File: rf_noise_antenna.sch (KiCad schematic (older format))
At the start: 41 parts, among them J1 Conn_Coaxial, J2 Conn_Coaxial, J3 Conn_01x03, J4 Raspberry_Pi_2_3, K1 MASWSS0115, K2 MASWSS0115, Q1 BC817, Q2 BC817, T1 MABA-009180-500MHz_1P_1S, U1 L7809

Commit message: Added measurmets
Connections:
- net at C11.1, C13.1, L4.2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: now also J3.2 (Pin_2); no longer J3.3 (Pin_3)
- net at C12.1, U1.1 (IN): now also J3.3 (Pin_3); no longer J3.2 (Pin_2)
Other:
- note added: "12V Power supply \nfor Active Antenna."
- note removed: "12V Powersupply for\n Active Antenna"
- moved on the sheet: C1, C10, C11, C12, C13, C14, C15, C2, C3, C4, C5, C6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

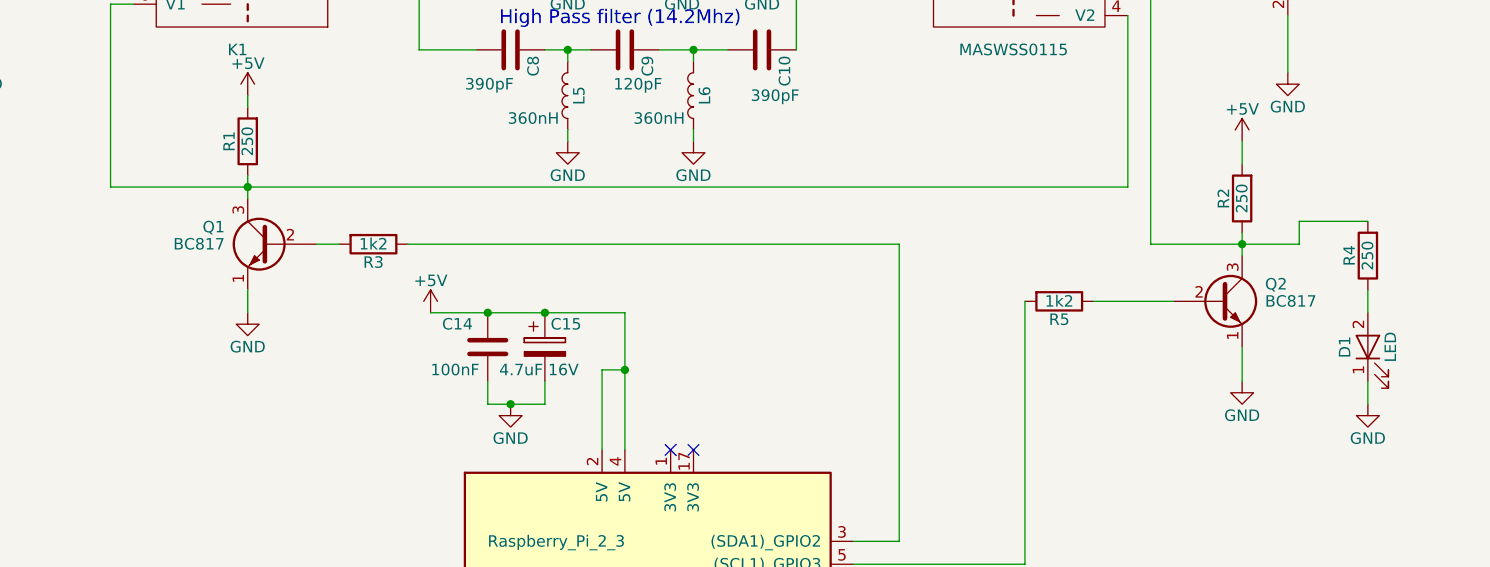
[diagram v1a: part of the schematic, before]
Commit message: Fix Transistor pin config
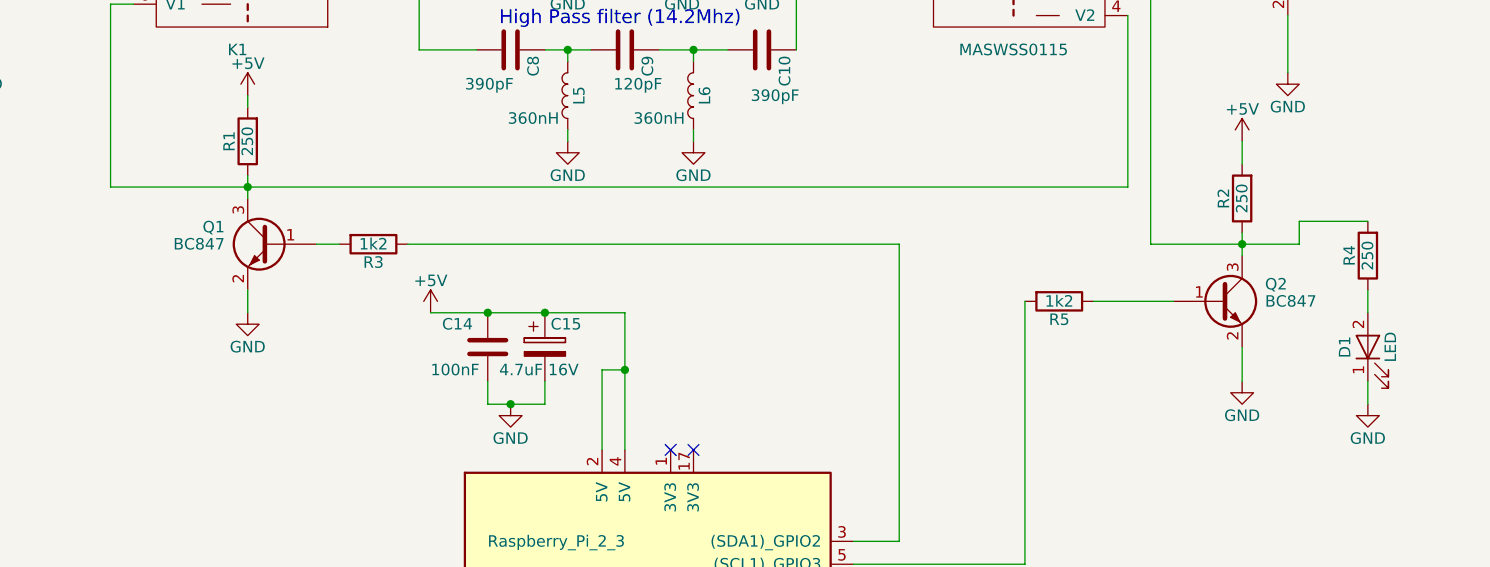
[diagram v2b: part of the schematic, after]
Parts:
- removed Q1, Q2: BC817, TO_SOT_Packages_SMD:SOT-23, symbol 2N2219
- added Q1, Q2: BC847, TO_SOT_Packages_SMD:SOT-23, symbol BC847
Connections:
- net GND: now also Q1.2 (E), Q2.2 (E)
- net at R5.1: now also Q2.1 (B)
- net at K1.4 (V2), K2.6 (V1), R2.1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: now also Q2.3 (C)
- net at K1.6 (V1), K2.4 (V2), R1.1: now also Q1.3 (C)
- net at R3.2: now also Q1.1 (B)
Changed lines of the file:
@@
-$EndComp
-$Comp
-L 2N2219 Q2
-U 1 1 5B76B57A
-P 9900 2650
-F 0 "Q2" H 10100 2725 50  0000 L CNN
-F 1 "BC817" H 10100 2650 50  0000 L CNN
-F 2 "TO_SOT_Packages_SMD:SOT-23" H 10100 2575 50  0001 L CIN
-F 3 "" H 9900 2650 50  0001 L CNN
-	1    9900 2650
-	1    0    0    -1
 $EndComp
 $Comp
@@
 $EndComp
 $Comp
-L 2N2219 Q1
-U 1 1 5B79A333
-P 5750 2400
-F 0 "Q1" H 5950 2475 50  0000 L CNN
-F 1 "BC817" H 5950 2400 50  0000 L CNN
-F 2 "TO_SOT_Packages_SMD:SOT-23" H 5950 2325 50  0001 L CIN
-F 3 "" H 5750 2400 50  0001 L CNN
-	1    5750 2400
-	-1   0    0    -1
-$EndComp
-$Comp
 L R R2
 U 1 1 5B79AFBD
@@
 Wire Wire Line
 	2050 1950 2250 1950
+$Comp
+L BC847 Q1
+U 1 1 5B831B5C
+P 5750 2400
+F 0 "Q1" H 5950 2475 50  0000 L CNN
+F 1 "BC847" H 5950 2400 50  0000 L CNN
+F 2 "TO_SOT_Packages_SMD:SOT-23" H 5950 2325 50  0001 L CIN
+F 3 "" H 5750 2400 50  0001 L CNN
+	1    5750 2400
+	-1   0    0    -1
+$EndComp
+$Comp
+L BC847 Q2
+U 1 1 5B83282F
+P 9900 2650
+F 0 "Q2" H 10100 2725 50  0000 L CNN
+F 1 "BC847" H 10100 2650 50  0000 L CNN
+F 2 "TO_SOT_Packages_SMD:SOT-23" H 10100 2575 50  0001 L CIN
+F 3 "" H 9900 2650 50  0001 L CNN
+	1    9900 2650
+	1    0    0    -1
+$EndComp
 $EndSCHEMATC

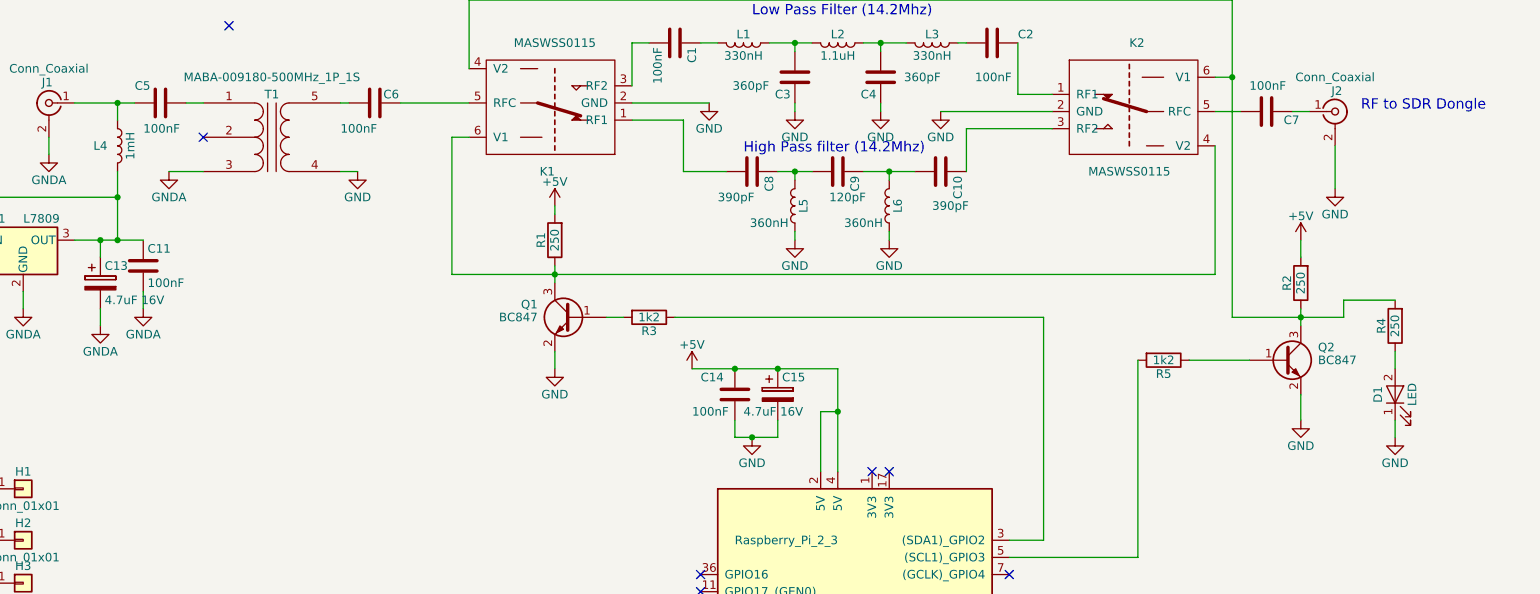
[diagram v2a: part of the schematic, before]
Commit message: Fix LED and Inductor value
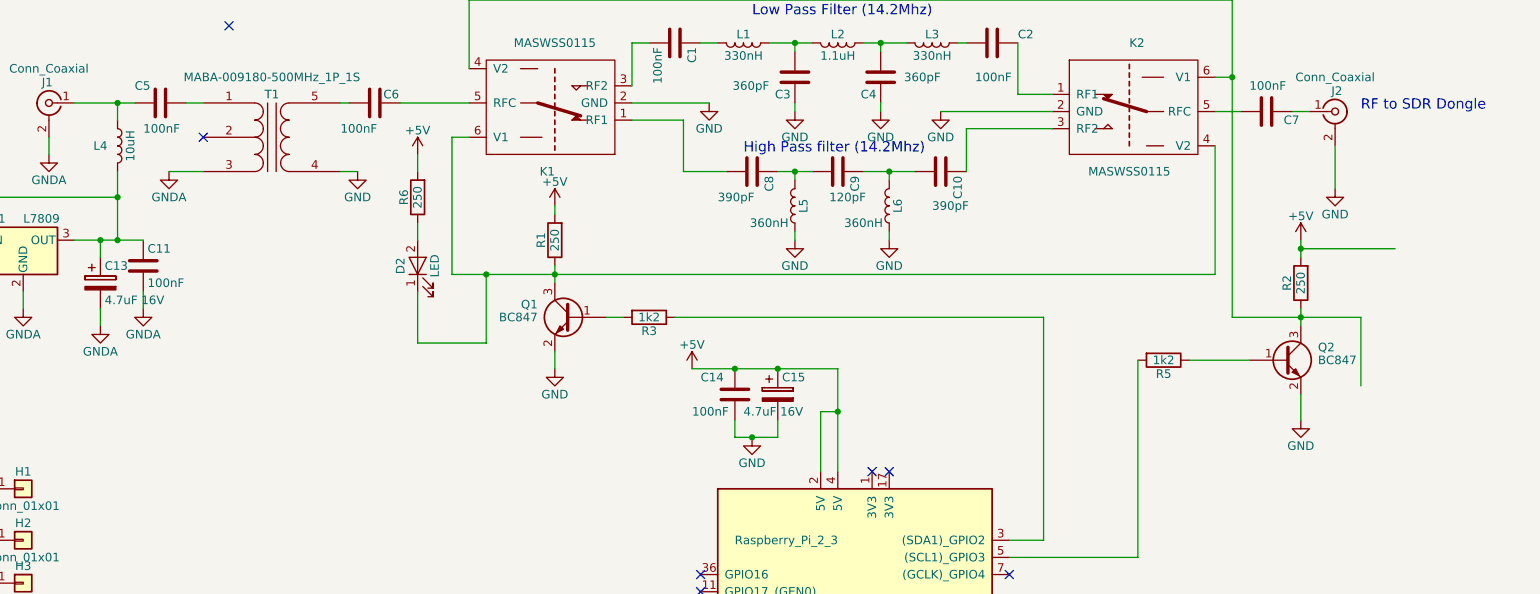
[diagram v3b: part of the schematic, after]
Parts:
- L4: value 1mH -> 10uH
- renumbered D1 to D2, R4 to R6
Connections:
- net +5V: now also R6.2
- net GND: no longer D2.1 (K)
- net at K1.4 (V2), K2.6 (V1), Q2.3 (C)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: no longer R6.2
- net at K1.6 (V1), K2.4 (V2), Q1.3 (C)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: now also D2.1 (K)
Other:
- moved on the sheet: D2, R6
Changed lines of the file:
@@
 P 3100 1400
 F 0 "L4" H 3000 1400 50  0000 C CNN
-F 1 "1mH" V 3175 1400 50  0000 C CNN
+F 1 "10uH" V 3175 1400 50  0000 C CNN
 F 2 "Inductors_SMD:L_0805_HandSoldering" H 3100 1400 50  0001 C CNN
 F 3 "" H 3100 1400 50  0001 C CNN
@@
 $EndComp
 $Comp
-L LED D1
+L LED D2
 U 1 1 5B76F22D
-P 10550 2850
-F 0 "D1" H 10550 2950 50  0000 C CNN
-F 1 "LED" H 10550 2750 50  0000 C CNN
-F 2 "LEDs:LED_0805_HandSoldering" H 10550 2850 50  0001 C CNN
-F 3 "" H 10550 2850 50  0001 C CNN
-	1    10550 2850
+P 4850 2100
+F 0 "D2" H 4850 2200 50  0000 C CNN
+F 1 "LED" H 4850 2000 50  0000 C CNN
+F 2 "LEDs:LED_0805_HandSoldering" H 4850 2100 50  0001 C CNN
+F 3 "" H 4850 2100 50  0001 C CNN
+	1    4850 2100
 	0    -1   -1   0
 $EndComp
 $Comp
-L R R4
+L R R6
 U 1 1 5B76F2C4
-P 10550 2450
-F 0 "R4" V 10630 2450 50  0000 C CNN
-F 1 "250" V 10550 2450 50  0000 C CNN
-F 2 "Resistors_SMD:R_0805_HandSoldering" V 10480 2450 50  0001 C CNN
-F 3 "" H 10550 2450 50  0001 C CNN
-	1    10550 2450
+P 4850 1700
+F 0 "R6" V 4930 1700 50  0000 C CNN
+F 1 "250" V 4850 1700 50  0000 C CNN
+F 2 "Resistors_SMD:R_0805_HandSoldering" V 4780 1700 50  0001 C CNN
+F 3 "" H 4850 1700 50  0001 C CNN
+	1    4850 1700
 	-1   0    0    1
 $EndComp
@@
 $EndComp
 $Comp
-L GND #PWR022
-U 1 1 5B79B67C
-P 10550 3100
-F 0 "#PWR022" H 10550 2850 50  0001 C CNN
-F 1 "GND" H 10550 2950 50  0000 C CNN
-F 2 "" H 10550 3100 50  0001 C CNN
-F 3 "" H 10550 3100 50  0001 C CNN
-	1    10550 3100
-	1    0    0    -1
-$EndComp
-$Comp
 L R R1
 U 1 1 5B79E16A
@@
 Wire Wire Line
 	9600 550  9600 2400
-Wire Wire Line
-	9600 2400 10250 2400
 Connection ~ 10000 2400
 Wire Wire Line
-	10250 2400 10250 2300
-Wire Wire Line
-	10250 2300 10550 2300
-Wire Wire Line
-	10550 2600 10550 2700
-Wire Wire Line
-	10550 3000 10550 3100
+	4850 1850 4850 1950
 Wire Wire Line
 	5650 2100 5650 2200
@@
 	1    0    0    -1
 $EndComp
+Wire Wire Line
+	9600 2400 10350 2400
+Wire Wire Line
+	4850 1550 4850 1450
+Wire Wire Line
+	10550 2000 10000 2000
+Connection ~ 10000 2000
+Wire Wire Line
+	10350 2400 10350 2800
+Wire Wire Line
+	4850 2250 4850 2550
+Wire Wire Line
+	4850 2550 5250 2550
+Wire Wire Line
+	5250 2550 5250 2150
+Connection ~ 5250 2150
+$Comp
+L +5V #PWR?
+U 1 1 5B84783A
+P 4850 1450
+F 0 "#PWR?" H 4850 1300 50  0001 C CNN
+F 1 "+5V" H 4850 1590 50  0000 C CNN
+F 2 "" H 4850 1450 50  0001 C CNN
+F 3 "" H 4850 1450 50  0001 C CNN
+	1    4850 1450
+	1    0    0    -1
+$EndComp

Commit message: Added Bom file
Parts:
- added D1: LED, LEDs:LED_0805_HandSoldering, symbol LED
- added R4: 250, Resistors_SMD:R_0805_HandSoldering, symbol R
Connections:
- net +5V: now also R4.2
- net at K1.4 (V2), K2.6 (V1), Q2.3 (C)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: now also D1.1 (K)
- new net: D1.2 (A), R4.1
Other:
- note added: "HPF"
- note added: "LPF"
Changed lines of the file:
@@
 	1    0    0    -1
 $EndComp
+$Comp
+L R R4
+U 1 1 5B8493CD
+P 10550 2150
+F 0 "R4" V 10630 2150 50  0000 C CNN
+F 1 "250" V 10550 2150 50  0000 C CNN
+F 2 "Resistors_SMD:R_0805_HandSoldering" V 10480 2150 50  0001 C CNN
+F 3 "" H 10550 2150 50  0001 C CNN
+	1    10550 2150
+	-1   0    0    1
+$EndComp
+$Comp
+L LED D1
+U 1 1 5B84949F
+P 10550 2600
+F 0 "D1" H 10550 2700 50  0000 C CNN
+F 1 "LED" H 10550 2500 50  0000 C CNN
+F 2 "LEDs:LED_0805_HandSoldering" H 10550 2600 50  0001 C CNN
+F 3 "" H 10550 2600 50  0001 C CNN
+	1    10550 2600
+	0    -1   -1   0
+$EndComp
+Wire Wire Line
+	10550 2300 10550 2450
+Wire Wire Line
+	10350 2800 10550 2800
+Wire Wire Line
+	10550 2800 10550 2750
+Text Notes 4600 2250 0    60   ~ 0
+HPF
+Text Notes 10700 2650 0    60   ~ 0
+LPF
 $EndSCHEMATC

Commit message: Added active Antenna
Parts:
- added AE?: Antenna, symbol Antenna
- added C?: 22uF, symbol CP
- added C? (x2): 100nF, symbol C
- added C?: 470nF Foil, symbol C
- added J?: SMA Edge, Connectors_Molex:Molex_SMA_Jack_Edge_Mount, symbol Conn_Coaxial
- added L?: 5Turns BN43-2402, symbol L
- added L?: 8 Turns BN73-202, symbol L
- added Q?: BF862, symbol Q_NJFET_DGS
- added Q?: 2N5583, TO_SOT_Packages_THT:TO-92_Molded_Narrow, symbol 2N3905
- added R?: 10M, symbol R
- added R? (x2): 1M, symbol R
- added R? (x2): 100, symbol R
- added R?: 100 0.5W, symbol R
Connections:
- net labels added: GNDPWR
- wire segments 105 -> 131
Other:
- note added: "12V"
- note added: "Block FM 88-108Mhz"
- note added: "Heatsink"
- note added: "Prevent VHF Oselation"

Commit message: Added anotation for active Antenna
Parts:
- U1: value L7809 -> L7812
- gave numbers to parts that had none: 16
